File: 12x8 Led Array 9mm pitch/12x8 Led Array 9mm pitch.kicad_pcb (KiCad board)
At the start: 4 copper layers, 140 x 120 mm, 310 parts, among them J1 LED ch 1-24, J2 LED ch 25-48, J3 LED ch 49-72, J4 LED ch 73-96, J5 logic/analog, U1 CD74HC4067M96, U2 CD74HC4067M96, U3 CD74HC4067M96, U4 CD74HC4067M96, U5 CD74HC4067M96, U6 CD74HC4067M96

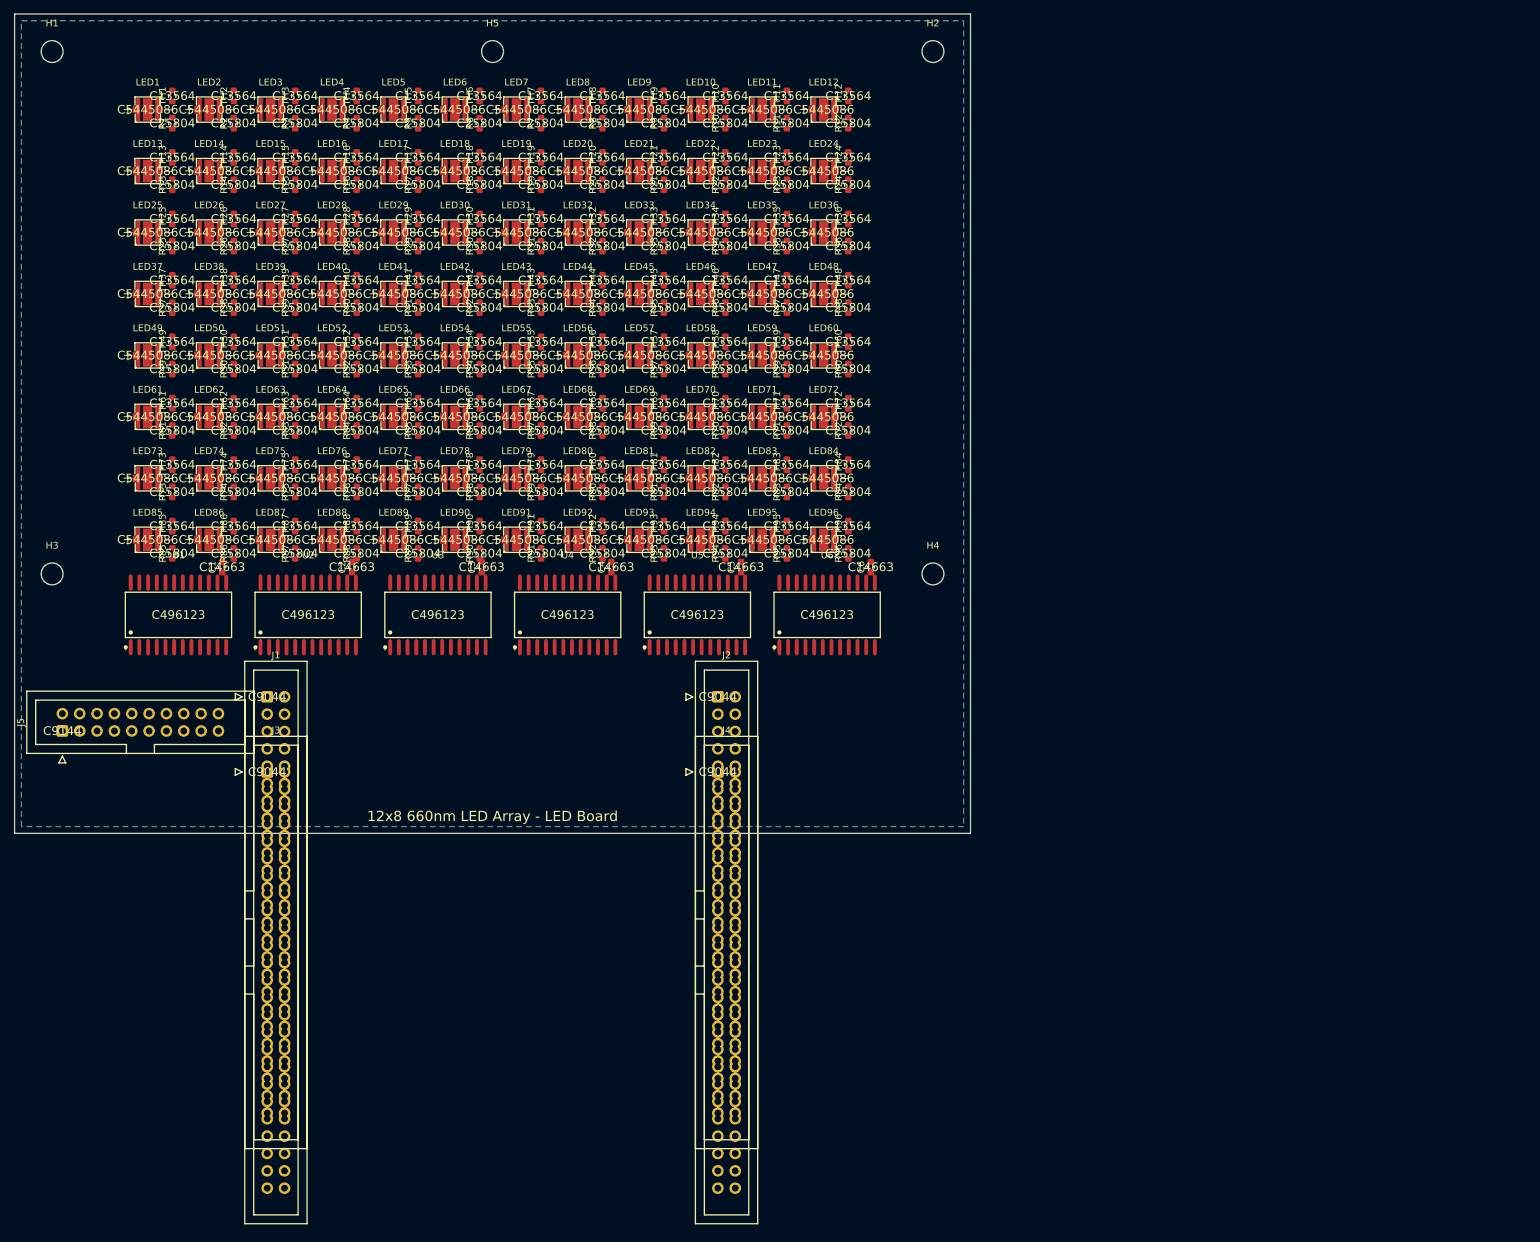
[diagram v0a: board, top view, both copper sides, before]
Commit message: Apply user's label cleanup style to control board
- All generated labels now carry explicit justification (left/right
  per rotation, bottom-anchored) matching the hand-cleaned LED board
- gen_schematics_hier.py takes led|ctl|all arg; LED board excluded
  from regeneration by default (hand-edited in KiCad)
- Control board netlist re-verified: all 412 nets match

Co-Authored-By: Claude Fable 5 <noreply@anthropic.com>
Claude-Session: https://claude.ai/code/session_017oD54uh7Tvu54u9NPQNcZB
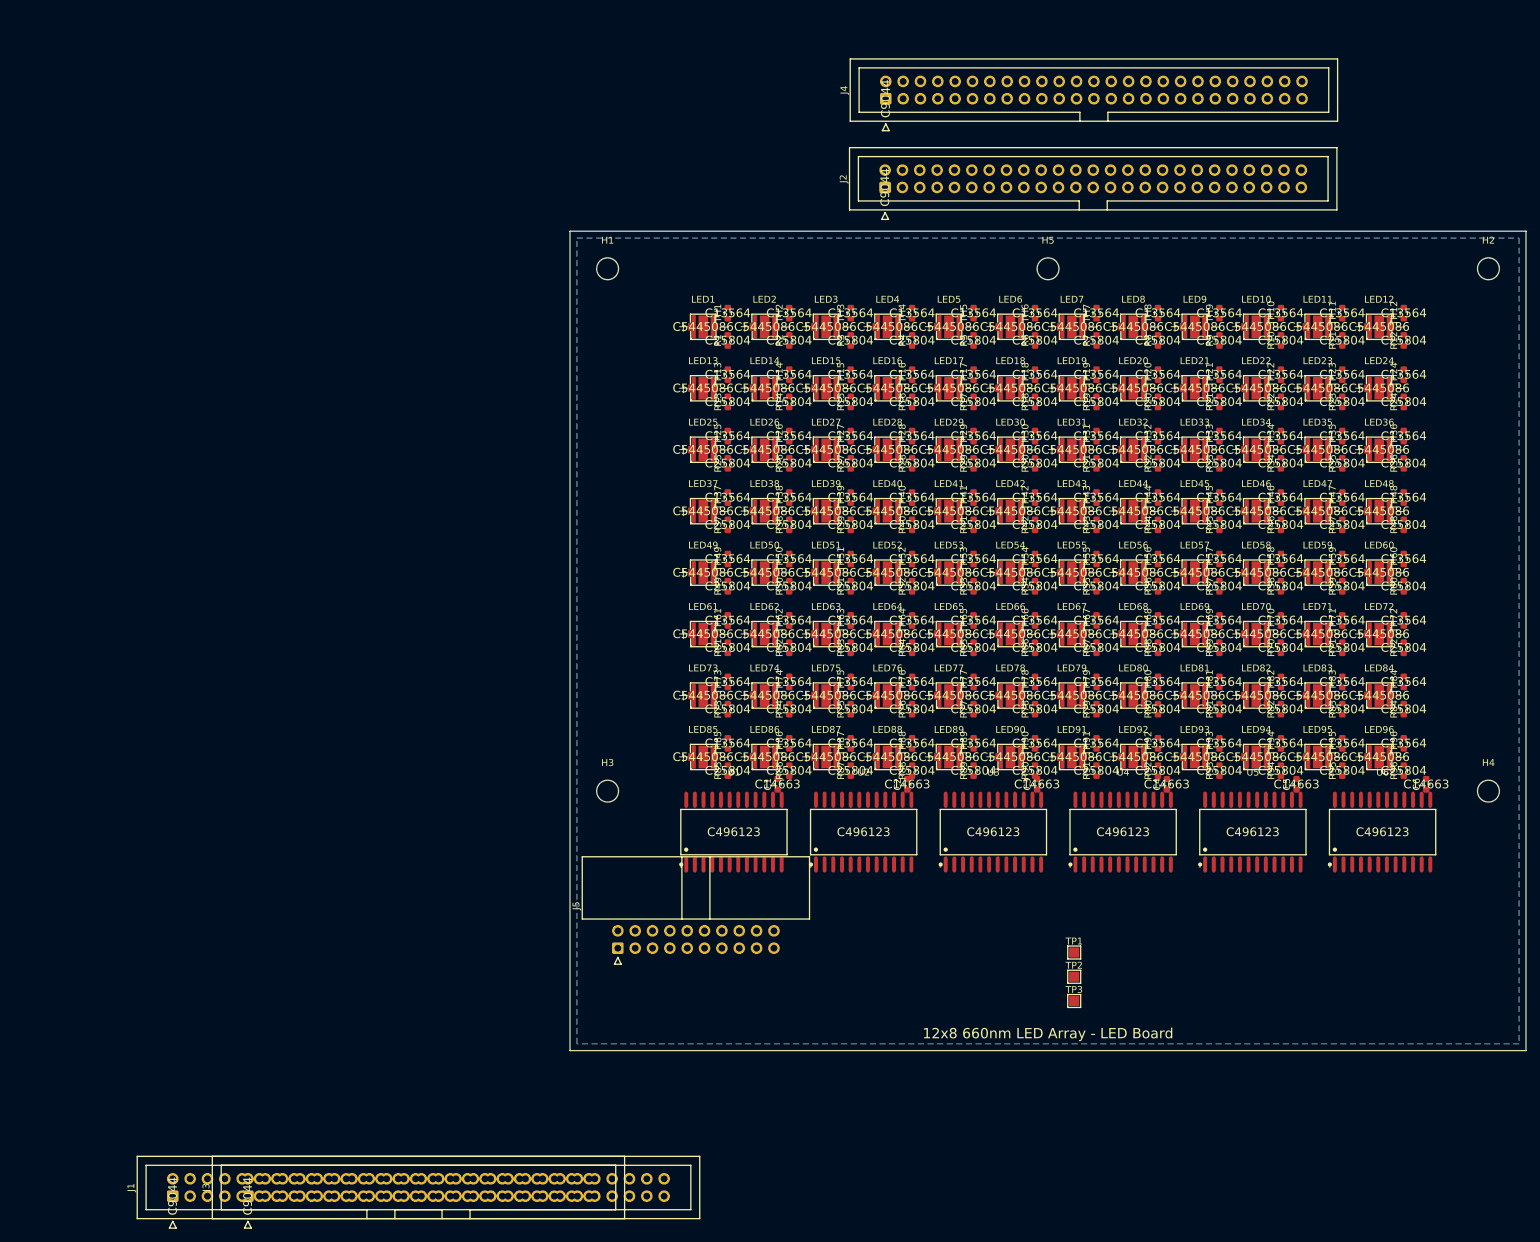
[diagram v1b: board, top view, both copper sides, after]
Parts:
- added TP1: +3V3, TestPoint:TestPoint_Pad_1.5x1.5mm, F.Cu at (155.2, 137.4)
- added TP2: GND, TestPoint:TestPoint_Pad_1.5x1.5mm, F.Cu at (155.2, 141.0)
- added TP3: GND, TestPoint:TestPoint_Pad_1.5x1.5mm, F.Cu at (155.2, 144.5)
- J5: footprint Connector_IDC:IDC-Header_2x10_P2.54mm_Vertical -> Connector_IDC:IDC-Header_2x10_P2.54mm_Horizontal
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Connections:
- C1 pad 1: (no net) -> +3.3V
- C1 pad 2: (no net) -> +3.3V
- C2 pad 1: (no net) -> +3.3V
- C2 pad 2: (no net) -> +3.3V
- C3 pad 1: (no net) -> +3.3V
- C3 pad 2: (no net) -> +3.3V
- C4 pad 1: (no net) -> +3.3V
- C4 pad 2: (no net) -> +3.3V
- C5 pad 1: (no net) -> +3.3V
- C5 pad 2: (no net) -> +3.3V
- C6 pad 1: (no net) -> +3.3V
- C6 pad 2: (no net) -> +3.3V
- J1 pad 1: (no net) -> /LED_A1
- J1 pad 10: (no net) -> /LED_K5
- J1 pad 11: (no net) -> /LED_A6
- J1 pad 12: (no net) -> /LED_K6
- J1 pad 13: (no net) -> /LED_A7
- J1 pad 14: (no net) -> /LED_K7
- J1 pad 15: (no net) -> /LED_A8
- J1 pad 16: (no net) -> /LED_K8
- J1 pad 17: (no net) -> /LED_A9
- J1 pad 18: (no net) -> /LED_K9
- J1 pad 19: (no net) -> /LED_A10
- J1 pad 2: (no net) -> /LED_K1
- J1 pad 20: (no net) -> /LED_K10
- J1 pad 21: (no net) -> /LED_A11
- J1 pad 22: (no net) -> /LED_K11
- J1 pad 23: (no net) -> /LED_A12
- J1 pad 24: (no net) -> /LED_K12
- J1 pad 25: (no net) -> /LED_A13
- J1 pad 26: (no net) -> /LED_K13
- J1 pad 27: (no net) -> /LED_A14
- J1 pad 28: (no net) -> /LED_K14
- J1 pad 29: (no net) -> /LED_A15
- J1 pad 3: (no net) -> /LED_A2
- J1 pad 30: (no net) -> /LED_K15
- J1 pad 31: (no net) -> /LED_A16
- J1 pad 32: (no net) -> /LED_K16
- J1 pad 33: (no net) -> /LED_A17
- J1 pad 34: (no net) -> /LED_K17
- J1 pad 35: (no net) -> /LED_A18
- J1 pad 36: (no net) -> /LED_K18
- J1 pad 37: (no net) -> /LED_A19
- J1 pad 38: (no net) -> /LED_K19
- J1 pad 39: (no net) -> /LED_A20
- J1 pad 4: (no net) -> /LED_K2
- J1 pad 40: (no net) -> /LED_K20
- J1 pad 41: (no net) -> /LED_A21
- J1 pad 42: (no net) -> /LED_K21
- J1 pad 43: (no net) -> /LED_A22
- J1 pad 44: (no net) -> /LED_K22
- J1 pad 45: (no net) -> /LED_A23
- J1 pad 46: (no net) -> /LED_K23
- J1 pad 47: (no net) -> /LED_A24
- J1 pad 48: (no net) -> /LED_K24
- J1 pad 49: (no net) -> +3.3V
- J1 pad 5: (no net) -> /LED_A3
- J1 pad 50: (no net) -> +3.3V
- J1 pad 6: (no net) -> /LED_K3
- J1 pad 7: (no net) -> /LED_A4
- J1 pad 8: (no net) -> /LED_K4
- J1 pad 9: (no net) -> /LED_A5
- J2 pad 1: (no net) -> /LED_A25
- J2 pad 10: (no net) -> /LED_K29
- J2 pad 11: (no net) -> /LED_A30
- J2 pad 12: (no net) -> /LED_K30
- J2 pad 13: (no net) -> /LED_A31
- J2 pad 14: (no net) -> /LED_K31
- J2 pad 15: (no net) -> /LED_A32
- J2 pad 16: (no net) -> /LED_K32
- J2 pad 17: (no net) -> /LED_A33
- J2 pad 18: (no net) -> /LED_K33
- J2 pad 19: (no net) -> /LED_A34
- J2 pad 2: (no net) -> /LED_K25
- J2 pad 20: (no net) -> /LED_K34
- J2 pad 21: (no net) -> /LED_A35
- J2 pad 22: (no net) -> /LED_K35
- J2 pad 23: (no net) -> /LED_A36
- J2 pad 24: (no net) -> /LED_K36
- J2 pad 25: (no net) -> /LED_A37
- J2 pad 26: (no net) -> /LED_K37
- J2 pad 27: (no net) -> /LED_A38
- J2 pad 28: (no net) -> /LED_K38
- J2 pad 29: (no net) -> /LED_A39
- J2 pad 3: (no net) -> /LED_A26
- J2 pad 30: (no net) -> /LED_K39
- J2 pad 31: (no net) -> /LED_A40
- J2 pad 32: (no net) -> /LED_K40
- J2 pad 33: (no net) -> /LED_A41
- J2 pad 34: (no net) -> /LED_K41
- J2 pad 35: (no net) -> /LED_A42
- J2 pad 36: (no net) -> /LED_K42
- J2 pad 37: (no net) -> /LED_A43
- J2 pad 38: (no net) -> /LED_K43
- J2 pad 39: (no net) -> /LED_A44
- J2 pad 4: (no net) -> /LED_K26
- J2 pad 40: (no net) -> /LED_K44
- J2 pad 41: (no net) -> /LED_A45
- J2 pad 42: (no net) -> /LED_K45
- J2 pad 43: (no net) -> /LED_A46
- J2 pad 44: (no net) -> /LED_K46
- J2 pad 45: (no net) -> /LED_A47
- J2 pad 46: (no net) -> /LED_K47
- J2 pad 47: (no net) -> /LED_A48
- J2 pad 48: (no net) -> /LED_K48
- J2 pad 49: (no net) -> +3.3V
- J2 pad 5: (no net) -> /LED_A27
- J2 pad 50: (no net) -> +3.3V
- J2 pad 6: (no net) -> /LED_K27
- J2 pad 7: (no net) -> /LED_A28
- J2 pad 8: (no net) -> /LED_K28
- J2 pad 9: (no net) -> /LED_A29
- J3 pad 1: (no net) -> /LED_A49
- J3 pad 10: (no net) -> /LED_K53
- J3 pad 11: (no net) -> /LED_A54
- J3 pad 12: (no net) -> /LED_K54
- J3 pad 13: (no net) -> /LED_A55
- J3 pad 14: (no net) -> /LED_K55
- J3 pad 15: (no net) -> /LED_A56
- J3 pad 16: (no net) -> /LED_K56
- J3 pad 17: (no net) -> /LED_A57
- J3 pad 18: (no net) -> /LED_K57
- J3 pad 19: (no net) -> /LED_A58
- J3 pad 2: (no net) -> /LED_K49
- J3 pad 20: (no net) -> /LED_K58
- J3 pad 21: (no net) -> /LED_A59
- J3 pad 22: (no net) -> /LED_K59
- J3 pad 23: (no net) -> /LED_A60
- J3 pad 24: (no net) -> /LED_K60
- J3 pad 25: (no net) -> /LED_A61
- J3 pad 26: (no net) -> /LED_K61
- J3 pad 27: (no net) -> /LED_A62
- J3 pad 28: (no net) -> /LED_K62
- J3 pad 29: (no net) -> /LED_A63
- J3 pad 3: (no net) -> /LED_A50
- J3 pad 30: (no net) -> /LED_K63
- J3 pad 31: (no net) -> /LED_A64
- J3 pad 32: (no net) -> /LED_K64
- J3 pad 33: (no net) -> /LED_A65
- J3 pad 34: (no net) -> /LED_K65
- J3 pad 35: (no net) -> /LED_A66
- J3 pad 36: (no net) -> /LED_K66
- J3 pad 37: (no net) -> /LED_A67
- J3 pad 38: (no net) -> /LED_K67
- J3 pad 39: (no net) -> /LED_A68
- J3 pad 4: (no net) -> /LED_K50
- J3 pad 40: (no net) -> /LED_K68
- J3 pad 41: (no net) -> /LED_A69
- J3 pad 42: (no net) -> /LED_K69
- J3 pad 43: (no net) -> /LED_A70
- J3 pad 44: (no net) -> /LED_K70
- J3 pad 45: (no net) -> /LED_A71
- J3 pad 46: (no net) -> /LED_K71
- J3 pad 47: (no net) -> /LED_A72
- J3 pad 48: (no net) -> /LED_K72
- J3 pad 49: (no net) -> +3.3V
- J3 pad 5: (no net) -> /LED_A51
- J3 pad 50: (no net) -> +3.3V
- J3 pad 6: (no net) -> /LED_K51
- J3 pad 7: (no net) -> /LED_A52
- J3 pad 8: (no net) -> /LED_K52
- J3 pad 9: (no net) -> /LED_A53
- J4 pad 1: (no net) -> /LED_A73
- J4 pad 10: (no net) -> /LED_K77
- J4 pad 11: (no net) -> /LED_A78
- J4 pad 12: (no net) -> /LED_K78
- J4 pad 13: (no net) -> /LED_A79
- J4 pad 14: (no net) -> /LED_K79
- J4 pad 15: (no net) -> /LED_A80
- J4 pad 16: (no net) -> /LED_K80
- J4 pad 17: (no net) -> /LED_A81
- J4 pad 18: (no net) -> /LED_K81
- J4 pad 19: (no net) -> /LED_A82
- J4 pad 2: (no net) -> /LED_K73
- J4 pad 20: (no net) -> /LED_K82
- J4 pad 21: (no net) -> /LED_A83
- J4 pad 22: (no net) -> /LED_K83
- J4 pad 23: (no net) -> /LED_A84
- J4 pad 24: (no net) -> /LED_K84
- J4 pad 25: (no net) -> /LED_A85
- J4 pad 26: (no net) -> /LED_K85
- J4 pad 27: (no net) -> /LED_A86
- J4 pad 28: (no net) -> /LED_K86
- J4 pad 29: (no net) -> /LED_A87
- J4 pad 3: (no net) -> /LED_A74
- J4 pad 30: (no net) -> /LED_K87
- J4 pad 31: (no net) -> /LED_A88
- J4 pad 32: (no net) -> /LED_K88
- J4 pad 33: (no net) -> /LED_A89
- J4 pad 34: (no net) -> /LED_K89
- J4 pad 35: (no net) -> /LED_A90
- J4 pad 36: (no net) -> /LED_K90
- J4 pad 37: (no net) -> /LED_A91
- J4 pad 38: (no net) -> /LED_K91
- J4 pad 39: (no net) -> /LED_A92
- J4 pad 4: (no net) -> /LED_K74
- J4 pad 40: (no net) -> /LED_K92
- J4 pad 41: (no net) -> /LED_A93
- J4 pad 42: (no net) -> /LED_K93
- J4 pad 43: (no net) -> /LED_A94
- J4 pad 44: (no net) -> /LED_K94
- J4 pad 45: (no net) -> /LED_A95
- J4 pad 46: (no net) -> /LED_K95
- J4 pad 47: (no net) -> /LED_A96
- J4 pad 48: (no net) -> /LED_K96
- J4 pad 49: (no net) -> +3.3V
- J4 pad 5: (no net) -> /LED_A75
- J4 pad 50: (no net) -> +3.3V
- J4 pad 6: (no net) -> /LED_K75
- J4 pad 7: (no net) -> /LED_A76
- J4 pad 8: (no net) -> /LED_K76
- J4 pad 9: (no net) -> /LED_A77
- J5 pad 1: (no net) -> +3.3V
- J5 pad 10: (no net) -> +3.3V
- J5 pad 11: (no net) -> /NTC_SIG5
- J5 pad 12: (no net) -> +3.3V
- J5 pad 13: (no net) -> /NTC_SIG6
- J5 pad 14: (no net) -> +3.3V
- J5 pad 15: (no net) -> /MUX_A0
- J5 pad 16: (no net) -> /MUX_A1
- J5 pad 17: (no net) -> /MUX_A2
- J5 pad 18: (no net) -> /MUX_A3
- J5 pad 19: (no net) -> +3.3V
- J5 pad 2: (no net) -> +3.3V
- J5 pad 20: (no net) -> +3.3V
- J5 pad 3: (no net) -> /NTC_SIG1
- J5 pad 4: (no net) -> +3.3V
- J5 pad 5: (no net) -> /NTC_SIG2
- J5 pad 6: (no net) -> +3.3V
- J5 pad 7: (no net) -> /NTC_SIG3
- J5 pad 8: (no net) -> +3.3V
- J5 pad 9: (no net) -> /NTC_SIG4
- LED1 pad 1: (no net) -> /LED_A1
- LED1 pad 2: (no net) -> /LED_K1
- LED1 pad 3: (no net) -> /LED_K1
- LED10 pad 1: (no net) -> /LED_A10
- LED10 pad 2: (no net) -> /LED_K10
- LED10 pad 3: (no net) -> /LED_K10
- LED11 pad 1: (no net) -> /LED_A11
- LED11 pad 2: (no net) -> /LED_K11
- LED11 pad 3: (no net) -> /LED_K11
- LED12 pad 1: (no net) -> /LED_A12
- LED12 pad 2: (no net) -> /LED_K12
- LED12 pad 3: (no net) -> /LED_K12
- LED13 pad 1: (no net) -> /LED_A13
- LED13 pad 2: (no net) -> /LED_K13
- LED13 pad 3: (no net) -> /LED_K13
- LED14 pad 1: (no net) -> /LED_A14
- LED14 pad 2: (no net) -> /LED_K14
- LED14 pad 3: (no net) -> /LED_K14
- LED15 pad 1: (no net) -> /LED_A15
- LED15 pad 2: (no net) -> /LED_K15
- LED15 pad 3: (no net) -> /LED_K15
- LED16 pad 1: (no net) -> /LED_A16
- LED16 pad 2: (no net) -> /LED_K16
- LED16 pad 3: (no net) -> /LED_K16
- LED17 pad 1: (no net) -> /LED_A17
- LED17 pad 2: (no net) -> /LED_K17
- LED17 pad 3: (no net) -> /LED_K17
- LED18 pad 1: (no net) -> /LED_A18
- LED18 pad 2: (no net) -> /LED_K18
- LED18 pad 3: (no net) -> /LED_K18
- LED19 pad 1: (no net) -> /LED_A19
- LED19 pad 2: (no net) -> /LED_K19
- LED19 pad 3: (no net) -> /LED_K19
- LED2 pad 1: (no net) -> /LED_A2
- LED2 pad 2: (no net) -> /LED_K2
- LED2 pad 3: (no net) -> /LED_K2
- LED20 pad 1: (no net) -> /LED_A20
- LED20 pad 2: (no net) -> /LED_K20
- LED20 pad 3: (no net) -> /LED_K20
- LED21 pad 1: (no net) -> /LED_A21
- LED21 pad 2: (no net) -> /LED_K21
- LED21 pad 3: (no net) -> /LED_K21
- LED22 pad 1: (no net) -> /LED_A22
- LED22 pad 2: (no net) -> /LED_K22
- LED22 pad 3: (no net) -> /LED_K22
- LED23 pad 1: (no net) -> /LED_A23
- LED23 pad 2: (no net) -> /LED_K23
- LED23 pad 3: (no net) -> /LED_K23
- LED24 pad 1: (no net) -> /LED_A24
- LED24 pad 2: (no net) -> /LED_K24
- LED24 pad 3: (no net) -> /LED_K24
- LED25 pad 1: (no net) -> /LED_A25
- LED25 pad 2: (no net) -> /LED_K25
- LED25 pad 3: (no net) -> /LED_K25
- LED26 pad 1: (no net) -> /LED_A26
- LED26 pad 2: (no net) -> /LED_K26
- LED26 pad 3: (no net) -> /LED_K26
- LED27 pad 1: (no net) -> /LED_A27
- LED27 pad 2: (no net) -> /LED_K27
- LED27 pad 3: (no net) -> /LED_K27
- LED28 pad 1: (no net) -> /LED_A28
- LED28 pad 2: (no net) -> /LED_K28
- LED28 pad 3: (no net) -> /LED_K28
- LED29 pad 1: (no net) -> /LED_A29
- LED29 pad 2: (no net) -> /LED_K29
- LED29 pad 3: (no net) -> /LED_K29
- LED3 pad 1: (no net) -> /LED_A3
- LED3 pad 2: (no net) -> /LED_K3
- LED3 pad 3: (no net) -> /LED_K3
- LED30 pad 1: (no net) -> /LED_A30
- LED30 pad 2: (no net) -> /LED_K30
- LED30 pad 3: (no net) -> /LED_K30
- LED31 pad 1: (no net) -> /LED_A31
- LED31 pad 2: (no net) -> /LED_K31
- LED31 pad 3: (no net) -> /LED_K31
- LED32 pad 1: (no net) -> /LED_A32
- LED32 pad 2: (no net) -> /LED_K32
- LED32 pad 3: (no net) -> /LED_K32
- LED33 pad 1: (no net) -> /LED_A33
- LED33 pad 2: (no net) -> /LED_K33
- LED33 pad 3: (no net) -> /LED_K33
- LED34 pad 1: (no net) -> /LED_A34
- LED34 pad 2: (no net) -> /LED_K34
- LED34 pad 3: (no net) -> /LED_K34
- LED35 pad 1: (no net) -> /LED_A35
- LED35 pad 2: (no net) -> /LED_K35
- LED35 pad 3: (no net) -> /LED_K35
- LED36 pad 1: (no net) -> /LED_A36
- LED36 pad 2: (no net) -> /LED_K36
- LED36 pad 3: (no net) -> /LED_K36
- LED37 pad 1: (no net) -> /LED_A37
- LED37 pad 2: (no net) -> /LED_K37
- LED37 pad 3: (no net) -> /LED_K37
- LED38 pad 1: (no net) -> /LED_A38
- LED38 pad 2: (no net) -> /LED_K38
- LED38 pad 3: (no net) -> /LED_K38
- LED39 pad 1: (no net) -> /LED_A39
- LED39 pad 2: (no net) -> /LED_K39
- LED39 pad 3: (no net) -> /LED_K39
- LED4 pad 1: (no net) -> /LED_A4
- LED4 pad 2: (no net) -> /LED_K4
- LED4 pad 3: (no net) -> /LED_K4
- LED40 pad 1: (no net) -> /LED_A40
- LED40 pad 2: (no net) -> /LED_K40
- LED40 pad 3: (no net) -> /LED_K40
- LED41 pad 1: (no net) -> /LED_A41
- LED41 pad 2: (no net) -> /LED_K41
- LED41 pad 3: (no net) -> /LED_K41
- LED42 pad 1: (no net) -> /LED_A42
- LED42 pad 2: (no net) -> /LED_K42
- LED42 pad 3: (no net) -> /LED_K42
- LED43 pad 1: (no net) -> /LED_A43
- LED43 pad 2: (no net) -> /LED_K43
- LED43 pad 3: (no net) -> /LED_K43
- LED44 pad 1: (no net) -> /LED_A44
- LED44 pad 2: (no net) -> /LED_K44
- LED44 pad 3: (no net) -> /LED_K44
- LED45 pad 1: (no net) -> /LED_A45
- LED45 pad 2: (no net) -> /LED_K45
- LED45 pad 3: (no net) -> /LED_K45
- LED46 pad 1: (no net) -> /LED_A46
- LED46 pad 2: (no net) -> /LED_K46
- LED46 pad 3: (no net) -> /LED_K46
- LED47 pad 1: (no net) -> /LED_A47
- LED47 pad 2: (no net) -> /LED_K47
- LED47 pad 3: (no net) -> /LED_K47
- LED48 pad 1: (no net) -> /LED_A48
- LED48 pad 2: (no net) -> /LED_K48
- LED48 pad 3: (no net) -> /LED_K48
- LED49 pad 1: (no net) -> /LED_A49
- LED49 pad 2: (no net) -> /LED_K49
- LED49 pad 3: (no net) -> /LED_K49
- LED5 pad 1: (no net) -> /LED_A5
- LED5 pad 2: (no net) -> /LED_K5
- LED5 pad 3: (no net) -> /LED_K5
- LED50 pad 1: (no net) -> /LED_A50
- LED50 pad 2: (no net) -> /LED_K50
- LED50 pad 3: (no net) -> /LED_K50
- LED51 pad 1: (no net) -> /LED_A51
- LED51 pad 2: (no net) -> /LED_K51
- LED51 pad 3: (no net) -> /LED_K51
- LED52 pad 1: (no net) -> /LED_A52
- LED52 pad 2: (no net) -> /LED_K52
- LED52 pad 3: (no net) -> /LED_K52
- LED53 pad 1: (no net) -> /LED_A53
- LED53 pad 2: (no net) -> /LED_K53
- LED53 pad 3: (no net) -> /LED_K53
- LED54 pad 1: (no net) -> /LED_A54
- LED54 pad 2: (no net) -> /LED_K54
- LED54 pad 3: (no net) -> /LED_K54
- LED55 pad 1: (no net) -> /LED_A55
- LED55 pad 2: (no net) -> /LED_K55
- LED55 pad 3: (no net) -> /LED_K55
- LED56 pad 1: (no net) -> /LED_A56
- LED56 pad 2: (no net) -> /LED_K56
- LED56 pad 3: (no net) -> /LED_K56
- LED57 pad 1: (no net) -> /LED_A57
- LED57 pad 2: (no net) -> /LED_K57
- LED57 pad 3: (no net) -> /LED_K57
- LED58 pad 1: (no net) -> /LED_A58
- LED58 pad 2: (no net) -> /LED_K58
- LED58 pad 3: (no net) -> /LED_K58
- LED59 pad 1: (no net) -> /LED_A59
- LED59 pad 2: (no net) -> /LED_K59
- LED59 pad 3: (no net) -> /LED_K59
- LED6 pad 1: (no net) -> /LED_A6
- LED6 pad 2: (no net) -> /LED_K6
- LED6 pad 3: (no net) -> /LED_K6
- LED60 pad 1: (no net) -> /LED_A60
- LED60 pad 2: (no net) -> /LED_K60
- LED60 pad 3: (no net) -> /LED_K60
- LED61 pad 1: (no net) -> /LED_A61
- LED61 pad 2: (no net) -> /LED_K61
- LED61 pad 3: (no net) -> /LED_K61
- LED62 pad 1: (no net) -> /LED_A62
- LED62 pad 2: (no net) -> /LED_K62
- LED62 pad 3: (no net) -> /LED_K62
- LED63 pad 1: (no net) -> /LED_A63
- LED63 pad 2: (no net) -> /LED_K63
- LED63 pad 3: (no net) -> /LED_K63
- LED64 pad 1: (no net) -> /LED_A64
- LED64 pad 2: (no net) -> /LED_K64
- LED64 pad 3: (no net) -> /LED_K64
- LED65 pad 1: (no net) -> /LED_A65
- LED65 pad 2: (no net) -> /LED_K65
- LED65 pad 3: (no net) -> /LED_K65
- LED66 pad 1: (no net) -> /LED_A66
- LED66 pad 2: (no net) -> /LED_K66
- LED66 pad 3: (no net) -> /LED_K66
- LED67 pad 1: (no net) -> /LED_A67
- LED67 pad 2: (no net) -> /LED_K67
- LED67 pad 3: (no net) -> /LED_K67
- LED68 pad 1: (no net) -> /LED_A68
- LED68 pad 2: (no net) -> /LED_K68
- LED68 pad 3: (no net) -> /LED_K68
- LED69 pad 1: (no net) -> /LED_A69
- LED69 pad 2: (no net) -> /LED_K69
- LED69 pad 3: (no net) -> /LED_K69
- LED7 pad 1: (no net) -> /LED_A7
- LED7 pad 2: (no net) -> /LED_K7
- LED7 pad 3: (no net) -> /LED_K7
- LED70 pad 1: (no net) -> /LED_A70
- LED70 pad 2: (no net) -> /LED_K70
- LED70 pad 3: (no net) -> /LED_K70
- LED71 pad 1: (no net) -> /LED_A71
- LED71 pad 2: (no net) -> /LED_K71
- LED71 pad 3: (no net) -> /LED_K71
- LED72 pad 1: (no net) -> /LED_A72
- LED72 pad 2: (no net) -> /LED_K72
- LED72 pad 3: (no net) -> /LED_K72
- LED73 pad 1: (no net) -> /LED_A73
- LED73 pad 2: (no net) -> /LED_K73
- LED73 pad 3: (no net) -> /LED_K73
- LED74 pad 1: (no net) -> /LED_A74
- LED74 pad 2: (no net) -> /LED_K74
- LED74 pad 3: (no net) -> /LED_K74
- LED75 pad 1: (no net) -> /LED_A75
- LED75 pad 2: (no net) -> /LED_K75
- LED75 pad 3: (no net) -> /LED_K75
- LED76 pad 1: (no net) -> /LED_A76
- LED76 pad 2: (no net) -> /LED_K76
- LED76 pad 3: (no net) -> /LED_K76
- LED77 pad 1: (no net) -> /LED_A77
- LED77 pad 2: (no net) -> /LED_K77
- LED77 pad 3: (no net) -> /LED_K77
- LED78 pad 1: (no net) -> /LED_A78
- LED78 pad 2: (no net) -> /LED_K78
- LED78 pad 3: (no net) -> /LED_K78
- LED79 pad 1: (no net) -> /LED_A79
- LED79 pad 2: (no net) -> /LED_K79
- LED79 pad 3: (no net) -> /LED_K79
- LED8 pad 1: (no net) -> /LED_A8
- LED8 pad 2: (no net) -> /LED_K8
- LED8 pad 3: (no net) -> /LED_K8
- LED80 pad 1: (no net) -> /LED_A80
- LED80 pad 2: (no net) -> /LED_K80
- LED80 pad 3: (no net) -> /LED_K80
- LED81 pad 1: (no net) -> /LED_A81
- LED81 pad 2: (no net) -> /LED_K81
- LED81 pad 3: (no net) -> /LED_K81
- LED82 pad 1: (no net) -> /LED_A82
- LED82 pad 2: (no net) -> /LED_K82
- LED82 pad 3: (no net) -> /LED_K82
- LED83 pad 1: (no net) -> /LED_A83
- LED83 pad 2: (no net) -> /LED_K83
- LED83 pad 3: (no net) -> /LED_K83
- LED84 pad 1: (no net) -> /LED_A84
- LED84 pad 2: (no net) -> /LED_K84
- LED84 pad 3: (no net) -> /LED_K84
- LED85 pad 1: (no net) -> /LED_A85
- LED85 pad 2: (no net) -> /LED_K85
- LED85 pad 3: (no net) -> /LED_K85
- LED86 pad 1: (no net) -> /LED_A86
- LED86 pad 2: (no net) -> /LED_K86
- LED86 pad 3: (no net) -> /LED_K86
- LED87 pad 1: (no net) -> /LED_A87
- LED87 pad 2: (no net) -> /LED_K87
- LED87 pad 3: (no net) -> /LED_K87
- LED88 pad 1: (no net) -> /LED_A88
- LED88 pad 2: (no net) -> /LED_K88
- LED88 pad 3: (no net) -> /LED_K88
- LED89 pad 1: (no net) -> /LED_A89
- LED89 pad 2: (no net) -> /LED_K89
- LED89 pad 3: (no net) -> /LED_K89
- LED9 pad 1: (no net) -> /LED_A9
- LED9 pad 2: (no net) -> /LED_K9
- LED9 pad 3: (no net) -> /LED_K9
- LED90 pad 1: (no net) -> /LED_A90
- LED90 pad 2: (no net) -> /LED_K90
- LED90 pad 3: (no net) -> /LED_K90
- LED91 pad 1: (no net) -> /LED_A91
- LED91 pad 2: (no net) -> /LED_K91
- LED91 pad 3: (no net) -> /LED_K91
- LED92 pad 1: (no net) -> /LED_A92
- LED92 pad 2: (no net) -> /LED_K92
- LED92 pad 3: (no net) -> /LED_K92
- LED93 pad 1: (no net) -> /LED_A93
- LED93 pad 2: (no net) -> /LED_K93
- LED93 pad 3: (no net) -> /LED_K93
- LED94 pad 1: (no net) -> /LED_A94
- LED94 pad 2: (no net) -> /LED_K94
- LED94 pad 3: (no net) -> /LED_K94
- LED95 pad 1: (no net) -> /LED_A95
- LED95 pad 2: (no net) -> /LED_K95
- LED95 pad 3: (no net) -> /LED_K95
- LED96 pad 1: (no net) -> /LED_A96
- LED96 pad 2: (no net) -> /LED_K96
- LED96 pad 3: (no net) -> /LED_K96
- R1 pad 1: (no net) -> /NTC1
- R1 pad 2: (no net) -> +3.3V
- R10 pad 1: (no net) -> /NTC10
- R10 pad 2: (no net) -> +3.3V
- R11 pad 1: (no net) -> /NTC11
- R11 pad 2: (no net) -> +3.3V
- R12 pad 1: (no net) -> /NTC12
- R12 pad 2: (no net) -> +3.3V
- R13 pad 1: (no net) -> /NTC13
- R13 pad 2: (no net) -> +3.3V
- R14 pad 1: (no net) -> /NTC14
- R14 pad 2: (no net) -> +3.3V
- R15 pad 1: (no net) -> /NTC15
- R15 pad 2: (no net) -> +3.3V
- R16 pad 1: (no net) -> /NTC16
- R16 pad 2: (no net) -> +3.3V
- R17 pad 1: (no net) -> /NTC17
- R17 pad 2: (no net) -> +3.3V
- R18 pad 1: (no net) -> /NTC18
- R18 pad 2: (no net) -> +3.3V
- R19 pad 1: (no net) -> /NTC19
- R19 pad 2: (no net) -> +3.3V
- R2 pad 1: (no net) -> /NTC2
- R2 pad 2: (no net) -> +3.3V
- R20 pad 1: (no net) -> /NTC20
- R20 pad 2: (no net) -> +3.3V
- R21 pad 1: (no net) -> /NTC21
- R21 pad 2: (no net) -> +3.3V
- R22 pad 1: (no net) -> /NTC22
- R22 pad 2: (no net) -> +3.3V
- R23 pad 1: (no net) -> /NTC23
- R23 pad 2: (no net) -> +3.3V
- R24 pad 1: (no net) -> /NTC24
- R24 pad 2: (no net) -> +3.3V
- R25 pad 1: (no net) -> /NTC25
- R25 pad 2: (no net) -> +3.3V
- R26 pad 1: (no net) -> /NTC26
- R26 pad 2: (no net) -> +3.3V
- R27 pad 1: (no net) -> /NTC27
- R27 pad 2: (no net) -> +3.3V
- R28 pad 1: (no net) -> /NTC28
- R28 pad 2: (no net) -> +3.3V
- R29 pad 1: (no net) -> /NTC29
- R29 pad 2: (no net) -> +3.3V
- R3 pad 1: (no net) -> /NTC3
- R3 pad 2: (no net) -> +3.3V
- R30 pad 1: (no net) -> /NTC30
- R30 pad 2: (no net) -> +3.3V
- R31 pad 1: (no net) -> /NTC31
- R31 pad 2: (no net) -> +3.3V
- R32 pad 1: (no net) -> /NTC32
- R32 pad 2: (no net) -> +3.3V
- R33 pad 1: (no net) -> /NTC33
- R33 pad 2: (no net) -> +3.3V
- R34 pad 1: (no net) -> /NTC34
- R34 pad 2: (no net) -> +3.3V
- R35 pad 1: (no net) -> /NTC35
- R35 pad 2: (no net) -> +3.3V
- R36 pad 1: (no net) -> /NTC36
- R36 pad 2: (no net) -> +3.3V
- R37 pad 1: (no net) -> /NTC37
- R37 pad 2: (no net) -> +3.3V
- R38 pad 1: (no net) -> /NTC38
- R38 pad 2: (no net) -> +3.3V
- R39 pad 1: (no net) -> /NTC39
- R39 pad 2: (no net) -> +3.3V
- R4 pad 1: (no net) -> /NTC4
- R4 pad 2: (no net) -> +3.3V
- R40 pad 1: (no net) -> /NTC40
- R40 pad 2: (no net) -> +3.3V
- R41 pad 1: (no net) -> /NTC41
- R41 pad 2: (no net) -> +3.3V
- R42 pad 1: (no net) -> /NTC42
- R42 pad 2: (no net) -> +3.3V
- R43 pad 1: (no net) -> /NTC43
- R43 pad 2: (no net) -> +3.3V
- R44 pad 1: (no net) -> /NTC44
- R44 pad 2: (no net) -> +3.3V
- R45 pad 1: (no net) -> /NTC45
- R45 pad 2: (no net) -> +3.3V
- R46 pad 1: (no net) -> /NTC46
- R46 pad 2: (no net) -> +3.3V
- R47 pad 1: (no net) -> /NTC47
- R47 pad 2: (no net) -> +3.3V
- R48 pad 1: (no net) -> /NTC48
- R48 pad 2: (no net) -> +3.3V
- R49 pad 1: (no net) -> /NTC49
- R49 pad 2: (no net) -> +3.3V
- R5 pad 1: (no net) -> /NTC5
- R5 pad 2: (no net) -> +3.3V
- R50 pad 1: (no net) -> /NTC50
- R50 pad 2: (no net) -> +3.3V
- R51 pad 1: (no net) -> /NTC51
- R51 pad 2: (no net) -> +3.3V
- R52 pad 1: (no net) -> /NTC52
- R52 pad 2: (no net) -> +3.3V
- R53 pad 1: (no net) -> /NTC53
- R53 pad 2: (no net) -> +3.3V
- R54 pad 1: (no net) -> /NTC54
- R54 pad 2: (no net) -> +3.3V
- R55 pad 1: (no net) -> /NTC55
- R55 pad 2: (no net) -> +3.3V
- R56 pad 1: (no net) -> /NTC56
- R56 pad 2: (no net) -> +3.3V
- R57 pad 1: (no net) -> /NTC57
- R57 pad 2: (no net) -> +3.3V
- R58 pad 1: (no net) -> /NTC58
- R58 pad 2: (no net) -> +3.3V
- R59 pad 1: (no net) -> /NTC59
- R59 pad 2: (no net) -> +3.3V
- R6 pad 1: (no net) -> /NTC6
- R6 pad 2: (no net) -> +3.3V
- R60 pad 1: (no net) -> /NTC60
- R60 pad 2: (no net) -> +3.3V
- R61 pad 1: (no net) -> /NTC61
- R61 pad 2: (no net) -> +3.3V
- R62 pad 1: (no net) -> /NTC62
- R62 pad 2: (no net) -> +3.3V
- R63 pad 1: (no net) -> /NTC63
- R63 pad 2: (no net) -> +3.3V
- R64 pad 1: (no net) -> /NTC64
- R64 pad 2: (no net) -> +3.3V
- R65 pad 1: (no net) -> /NTC65
- R65 pad 2: (no net) -> +3.3V
- R66 pad 1: (no net) -> /NTC66
- R66 pad 2: (no net) -> +3.3V
- R67 pad 1: (no net) -> /NTC67
- R67 pad 2: (no net) -> +3.3V
- R68 pad 1: (no net) -> /NTC68
- R68 pad 2: (no net) -> +3.3V
- R69 pad 1: (no net) -> /NTC69
- R69 pad 2: (no net) -> +3.3V
- R7 pad 1: (no net) -> /NTC7
- R7 pad 2: (no net) -> +3.3V
- R70 pad 1: (no net) -> /NTC70
- R70 pad 2: (no net) -> +3.3V
- R71 pad 1: (no net) -> /NTC71
- R71 pad 2: (no net) -> +3.3V
- R72 pad 1: (no net) -> /NTC72
- R72 pad 2: (no net) -> +3.3V
- R73 pad 1: (no net) -> /NTC73
- R73 pad 2: (no net) -> +3.3V
- R74 pad 1: (no net) -> /NTC74
- R74 pad 2: (no net) -> +3.3V
- R75 pad 1: (no net) -> /NTC75
- R75 pad 2: (no net) -> +3.3V
- R76 pad 1: (no net) -> /NTC76
- R76 pad 2: (no net) -> +3.3V
- R77 pad 1: (no net) -> /NTC77
- R77 pad 2: (no net) -> +3.3V
- R78 pad 1: (no net) -> /NTC78
- R78 pad 2: (no net) -> +3.3V
- R79 pad 1: (no net) -> /NTC79
- R79 pad 2: (no net) -> +3.3V
- R8 pad 1: (no net) -> /NTC8
- R8 pad 2: (no net) -> +3.3V
- R80 pad 1: (no net) -> /NTC80
- R80 pad 2: (no net) -> +3.3V
- R81 pad 1: (no net) -> /NTC81
- R81 pad 2: (no net) -> +3.3V
- R82 pad 1: (no net) -> /NTC82
- R82 pad 2: (no net) -> +3.3V
- R83 pad 1: (no net) -> /NTC83
- R83 pad 2: (no net) -> +3.3V
- R84 pad 1: (no net) -> /NTC84
- R84 pad 2: (no net) -> +3.3V
- R85 pad 1: (no net) -> /NTC85
- R85 pad 2: (no net) -> +3.3V
- R86 pad 1: (no net) -> /NTC86
- R86 pad 2: (no net) -> +3.3V
- R87 pad 1: (no net) -> /NTC87
- R87 pad 2: (no net) -> +3.3V
- R88 pad 1: (no net) -> /NTC88
- R88 pad 2: (no net) -> +3.3V
- R89 pad 1: (no net) -> /NTC89
- R89 pad 2: (no net) -> +3.3V
- R9 pad 1: (no net) -> /NTC9
- R9 pad 2: (no net) -> +3.3V
- R90 pad 1: (no net) -> /NTC90
- R90 pad 2: (no net) -> +3.3V
- R91 pad 1: (no net) -> /NTC91
- R91 pad 2: (no net) -> +3.3V
- R92 pad 1: (no net) -> /NTC92
- R92 pad 2: (no net) -> +3.3V
- R93 pad 1: (no net) -> /NTC93
- R93 pad 2: (no net) -> +3.3V
- R94 pad 1: (no net) -> /NTC94
- R94 pad 2: (no net) -> +3.3V
- R95 pad 1: (no net) -> /NTC95
- R95 pad 2: (no net) -> +3.3V
- R96 pad 1: (no net) -> /NTC96
- R96 pad 2: (no net) -> +3.3V
- TH1 pad 1: (no net) -> +3V3
- TH1 pad 2: (no net) -> /NTC1
- TH10 pad 1: (no net) -> +3V3
- TH10 pad 2: (no net) -> /NTC10
- TH11 pad 1: (no net) -> +3V3
- TH11 pad 2: (no net) -> /NTC11
- TH12 pad 1: (no net) -> +3V3
- TH12 pad 2: (no net) -> /NTC12
- TH13 pad 1: (no net) -> +3V3
- TH13 pad 2: (no net) -> /NTC13
- TH14 pad 1: (no net) -> +3V3
- TH14 pad 2: (no net) -> /NTC14
- TH15 pad 1: (no net) -> +3V3
- TH15 pad 2: (no net) -> /NTC15
- TH16 pad 1: (no net) -> +3V3
- TH16 pad 2: (no net) -> /NTC16
- TH17 pad 1: (no net) -> +3V3
- TH17 pad 2: (no net) -> /NTC17
- TH18 pad 1: (no net) -> +3V3
- TH18 pad 2: (no net) -> /NTC18
- TH19 pad 1: (no net) -> +3V3
- TH19 pad 2: (no net) -> /NTC19
- TH2 pad 1: (no net) -> +3V3
- TH2 pad 2: (no net) -> /NTC2
- TH20 pad 1: (no net) -> +3V3
- TH20 pad 2: (no net) -> /NTC20
- TH21 pad 1: (no net) -> +3V3
- TH21 pad 2: (no net) -> /NTC21
- TH22 pad 1: (no net) -> +3V3
- TH22 pad 2: (no net) -> /NTC22
- TH23 pad 1: (no net) -> +3V3
- TH23 pad 2: (no net) -> /NTC23
- TH24 pad 1: (no net) -> +3V3
- TH24 pad 2: (no net) -> /NTC24
- TH25 pad 1: (no net) -> +3V3
- TH25 pad 2: (no net) -> /NTC25
- TH26 pad 1: (no net) -> +3V3
- TH26 pad 2: (no net) -> /NTC26
- TH27 pad 1: (no net) -> +3V3
- TH27 pad 2: (no net) -> /NTC27
- TH28 pad 1: (no net) -> +3V3
- TH28 pad 2: (no net) -> /NTC28
- TH29 pad 1: (no net) -> +3V3
- TH29 pad 2: (no net) -> /NTC29
- TH3 pad 1: (no net) -> +3V3
- TH3 pad 2: (no net) -> /NTC3
- TH30 pad 1: (no net) -> +3V3
- TH30 pad 2: (no net) -> /NTC30
- TH31 pad 1: (no net) -> +3V3
- TH31 pad 2: (no net) -> /NTC31
- TH32 pad 1: (no net) -> +3V3
- TH32 pad 2: (no net) -> /NTC32
- TH33 pad 1: (no net) -> +3V3
- TH33 pad 2: (no net) -> /NTC33
- TH34 pad 1: (no net) -> +3V3
- TH34 pad 2: (no net) -> /NTC34
- TH35 pad 1: (no net) -> +3V3
- TH35 pad 2: (no net) -> /NTC35
- TH36 pad 1: (no net) -> +3V3
- TH36 pad 2: (no net) -> /NTC36
- TH37 pad 1: (no net) -> +3V3
- TH37 pad 2: (no net) -> /NTC37
- TH38 pad 1: (no net) -> +3V3
- TH38 pad 2: (no net) -> /NTC38
- TH39 pad 1: (no net) -> +3V3
- TH39 pad 2: (no net) -> /NTC39
- TH4 pad 1: (no net) -> +3V3
- TH4 pad 2: (no net) -> /NTC4
- TH40 pad 1: (no net) -> +3V3
- TH40 pad 2: (no net) -> /NTC40
- TH41 pad 1: (no net) -> +3V3
- TH41 pad 2: (no net) -> /NTC41
- TH42 pad 1: (no net) -> +3V3
- TH42 pad 2: (no net) -> /NTC42
- TH43 pad 1: (no net) -> +3V3
- TH43 pad 2: (no net) -> /NTC43
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
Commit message: Optimize ribbon/mux pin assignments to match user's PCB placement
- Quadrant mapping from actual footprint positions (via pcbnew API):
  J1 left-back = cols1-6/rows1-4, J2 right-back = cols7-12/rows1-4,
  J4 left-front = cols1-6/rows5-8, J3 right-front = cols7-12/rows5-8;
  pin pairs column-major in physical pin-1 direction (nested fan-out,
  no crossings)
- NTC->mux side-matched: U1-U3 serve cols 1-6, U6/U5/U4 cols 7-12
- pin_maps.py generated by optimize_pins.py; design_data now table-driven
- 274 labels renamed in the hand-edited LED sch (proximity-matched,
  0 misses); control board regenerated; CONNECTIONS.md updated
- Both netlists verify (300+412 nets), LED ERC still 0 errors

Co-Authored-By: Claude Fable 5 <noreply@anthropic.com>
Claude-Session: https://claude.ai/code/session_017oD54uh7Tvu54u9NPQNcZB
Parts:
- moved H2 211.3 mm to (423.4, -2.46)
- moved H4 211.3 mm to (423.4, 74.0)
- moved H5 211.3 mm to (358.9, -2.46)
- moved H3 160.7 mm to (225.6, 32.8)
- moved J4 130.8 mm to (82.9, 135.3)
- moved J3 126.8 mm to (155.2, 135.3)
- moved J2 125.2 mm to (155.2, 147.5)
- moved TP3 78.6 mm to (228.4, 116.0)
- moved U3 74.3 mm to (70.5, 105.2), turned to -90 degrees
- moved U1 73.0 mm to (70.2, 55.8), turned to -90 degrees
- moved C3 72.3 mm to (77.5, 111.6), turned to 0 degrees
- moved TP1 71.2 mm to (224.8, 122.4)
- moved TP2 70.8 mm to (221.4, 115.8)
- moved U6 69.9 mm to (228.4, 55.8), turned to 90 degrees
- moved U4 67.7 mm to (228.4, 105.2), turned to 90 degrees
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
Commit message: LED board outline + placement fixes for user's layout
- Rounded-rect Edge.Cuts (195 x 131.8mm) fenced around actual
  footprint extents; old draft outline removed
- Stray holes H2/H4/H5 relocated inside the new outline
- Mux decoupling caps C1-C6 nudged 3.5mm outboard (pads overlapped
  mux pin rows - 6 shorts + 6 clearance violations resolved)
- DRC now silk-cosmetics only

Co-Authored-By: Claude Fable 5 <noreply@anthropic.com>
Claude-Session: https://claude.ai/code/session_017oD54uh7Tvu54u9NPQNcZB
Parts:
- moved H2 393.6 mm to (52.0, 128.0)
- moved H5 308.8 mm to (52.0, 32.0)
- moved H4 198.8 mm to (232.0, 128.0)
- moved C1 3.50 mm to (80.7, 62.2)
- moved C2 3.50 mm to (81.0, 86.7)
- moved C3 3.50 mm to (81.0, 111.6)
- moved C4 3.50 mm to (217.9, 98.8)
- moved C5 3.50 mm to (217.9, 73.9)
- moved C6 3.50 mm to (217.9, 49.4)
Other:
- board size 140 x 120 mm -> 195 x 131.8 mm
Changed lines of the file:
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@@
 	(footprint "Capacitor_SMD:C_0603_1608Metric"
 		(layer "F.Cu")
-		(at 221.44 49.44 180)
+		(at 217.94 49.44 180)
 		(descr "Capacitor SMD 0603 (1608 Metric), square (rectangular) end terminal, IPC-7351 nominal, (Body size source: IPC-SM-782 page 76, https://www.pcb-3d.com/wordpress/wp-content/uploads/ipc-sm-782a_amendment_1_and_2.pdf)")
 		(tags "capacitor")
@@
 	(footprint "Capacitor_SMD:C_0603_1608Metric"
 		(layer "F.Cu")
-		(at 221.44 73.89 180)
+		(at 217.94 73.89 180)
 		(descr "Capacitor SMD 0603 (1608 Metric), square (rectangular) end terminal, IPC-7351 nominal, (Body size source: IPC-SM-782 page 76, https://www.pcb-3d.com/wordpress/wp-content/uploads/ipc-sm-782a_amendment_1_and_2.pdf)")
 		(tags "capacitor")
@@
 	(footprint "MountingHole:MountingHole_3.2mm_M3"
 		(layer "F.Cu")
-		(at 423.36 -2.46)
+		(at 52 128)
 		(descr "Mounting Hole 3.2mm, M3, no annular, generated by kicad-footprint-generator mountinghole.py")
 		(tags "mountinghole M3")
@@
 	(footprint "MountingHole:MountingHole_3.2mm_M3"
 		(layer "F.Cu")
-		(at 423.36 74.04)
+		(at 232 128)
 		(descr "Mounting Hole 3.2mm, M3, no annular, generated by kicad-footprint-generator mountinghole.py")
 		(tags "mountinghole M3")
@@
 	(footprint "Capacitor_SMD:C_0603_1608Metric"
 		(layer "F.Cu")
-		(at 221.44 98.81 180)
+		(at 217.94 98.81 180)
 		(descr "Capacitor SMD 0603 (1608 Metric), square (rectangular) end terminal, IPC-7351 nominal, (Body size source: IPC-SM-782 page 76, https://www.pcb-3d.com/wordpress/wp-content/uploads/ipc-sm-782a_amendment_1_and_2.pdf)")
 		(tags "capacitor")
@@
 	(footprint "MountingHole:MountingHole_3.2mm_M3"
 		(layer "F.Cu")
-		(at 358.86 -2.46)
+		(at 52 32)
 		(descr "Mounting Hole 3.2mm, M3, no annular, generated by kicad-footprint-generator mountinghole.py")
 		(tags "mountinghole M3")
@@
 	(footprint "Capacitor_SMD:C_0603_1608Metric"
 		(layer "F.Cu")
-		(at 77.48 86.69)
+		(at 80.98 86.69)
 		(descr "Capacitor SMD 0603 (1608 Metric), square (rectangular) end terminal, IPC-7351 nominal, (Body size source: IPC-SM-782 page 76, https://www.pcb-3d.com/wordpress/wp-content/uploads/ipc-sm-782a_amendment_1_and_2.pdf)")
 		(tags "capacitor")
@@
 	(footprint "Capacitor_SMD:C_0603_1608Metric"
 		(layer "F.Cu")
-		(at 77.22 62.24)
+		(at 80.72 62.24)
 		(descr "Capacitor SMD 0603 (1608 Metric), square (rectangular) end terminal, IPC-7351 nominal, (Body size source: IPC-SM-782 page 76, https://www.pcb-3d.com/wordpress/wp-content/uploads/ipc-sm-782a_amendment_1_and_2.pdf)")
 		(tags "capacitor")
@@
 	(footprint "Capacitor_SMD:C_0603_1608Metric"
 		(layer "F.Cu")
-		(at 77.48 111.61)
+		(at 80.98 111.61)
 		(descr "Capacitor SMD 0603 (1608 Metric), square (rectangular) end terminal, IPC-7351 nominal, (Body size source: IPC-SM-782 page 76, https://www.pcb-3d.com/wordpress/wp-content/uploads/ipc-sm-782a_amendment_1_and_2.pdf)")
 		(tags "capacitor")
@@
 		)
 	)
-	(gr_rect
-		(start 288.86 -7.96)
-		(end 428.86 112.04)
+	(gr_arc
+		(start 44.5 27.5)
+		(mid 45.37868 25.37868)
+		(end 47.5 24.5)
+		(stroke
+			(width 0.1)
+			(type default)
+		)
+		(layer "Edge.Cuts")
+	)
+	(gr_line
+		(start 44.5 153.3)
+		(end 44.5 27.5)
+		(stroke
+			(width 0.1)
+			(type default)
+		)
+		(layer "Edge.Cuts")
+	)
+	(gr_line
+		(start 47.5 24.5)
+		(end 236.5 24.5)
+		(stroke
+			(width 0.1)
+			(type default)
+		)
+		(layer "Edge.Cuts")
+	)
+	(gr_arc
+		(start 47.5 156.3)
+		(mid 45.37868 155.42132)
+		(end 44.5 153.3)
+		(stroke
+			(width 0.1)
+			(type default)
+		)
+		(layer "Edge.Cuts")
+	)
+	(gr_arc
+		(start 236.5 24.5)
+		(mid 238.62132 25.37868)
+		(end 239.5 27.5)
+		(stroke
+			(width 0.1)
+			(type default)
+		)
+		(layer "Edge.Cuts")
+	)
+	(gr_line
+		(start 236.5 156.3)
+		(end 47.5 156.3)
+		(stroke
+			(width 0.1)
+			(type default)
+		)
+		(layer "Edge.Cuts")
+	)
+	(gr_line
+		(start 239.5 27.5)
+		(end 239.5 153.3)
+		(stroke
+			(width 0.1)
+			(type default)
+		)
+		(layer "Edge.Cuts")
+	)
+	(gr_arc
+		(start 239.5 153.3)
+		(mid 238.62132 155.42132)
+		(end 236.5 156.3)
 		(stroke
 			(width 0.1)
 			(type default)
 		)
-		(fill no)
 		(layer "Edge.Cuts")
 	)
